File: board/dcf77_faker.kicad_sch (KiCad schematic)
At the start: 46 parts, among them J1 Barrel_Jack, J2 DBG, J3 ANT, J4 LCD_I2C, SW1 RST, SW2 H, SW3 MIN, SW4 S, U1 NCP1117ST33T3G, U2 ATSAML21G18B-AUT, X1 32.768kHz, X2 31MHz

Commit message: hand-solder X2, fix newly-detected DRC violations
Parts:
- X2: footprint Oscillator_Microchip:Oscillator_SMD_Microchip_DSC8001A-6Pin_7.0x5.0mm -> Oscillator_Microchip:Oscillator_SMD_Microchip_DSC8001A-6Pin_7.0x5.0mm_HandSolder
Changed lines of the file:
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@@
 (kicad_sch (version 20230121) (generator eeschema)
   (paper "A4")
+  (bus_alias "VIN" (members "VDDIN" "VSW" "VDDCORE" "VDDIO1" "VDDIO2" "VDDANA"))
+  (bus_alias "SWD" (members "SWDIO" "SWCLK" "~{RST}"))
   (bus_alias "BTN" (members "H" "MIN" "S"))
-  (bus_alias "VIN" (members "VDDIN" "VSW" "VDDCORE" "VDDIO1" "VDDIO2" "VDDANA"))
   (bus_alias "TWI0" (members "SDA0" "SCL0"))
-  (bus_alias "SWD" (members "SWDIO" "SWCLK" "~{RST}"))
   (junction (at 251.46 45.72) (diameter 0) (color 0 0 0 0)
   )
@@
       (effects (font (size 1.27 1.27)))
     )
-    (property "Footprint" "Oscillator_Microchip:Oscillator_SMD_Microchip_DSC8001A-6Pin_7.0x5.0mm" (at 243.84 130.81 0)
-      (effects (font (size 1.27 1.27)) hide)
-    )
+    (property "Footprint" "Oscillator_Microchip:Oscillator_SMD_Microchip_DSC8001A-6Pin_7.0x5.0mm_HandSolder" (at 243.84 130.81 0)
+      (effects (font (size 1.27 1.27)) hide)
+    )

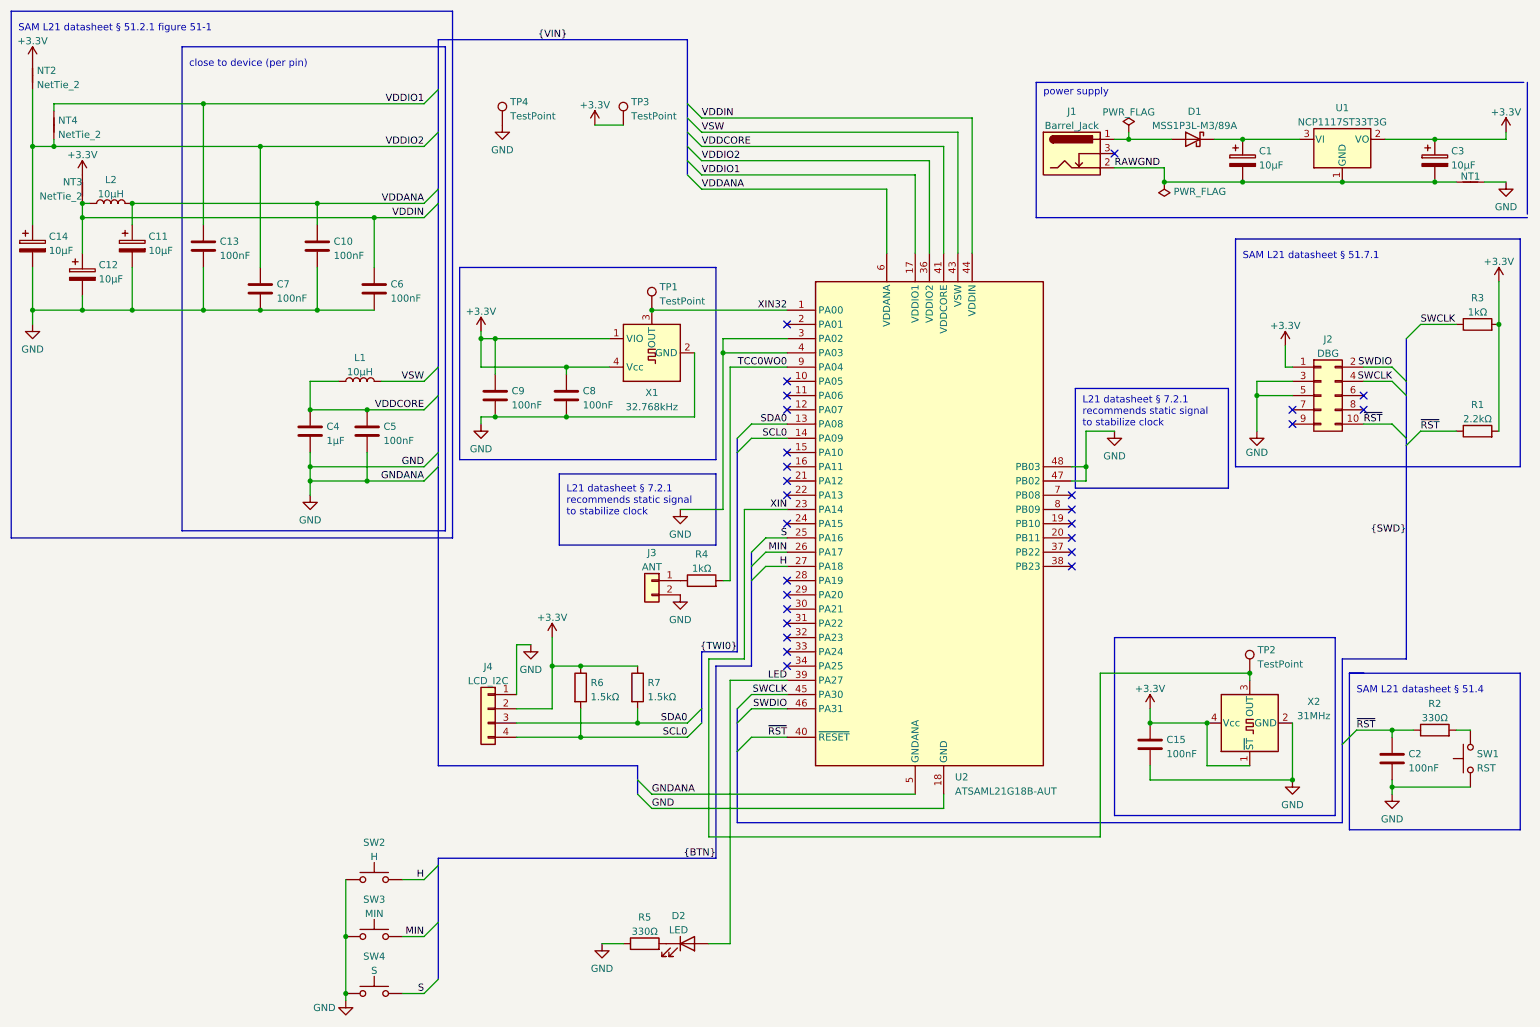
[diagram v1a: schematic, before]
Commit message: board: allow disabling X2
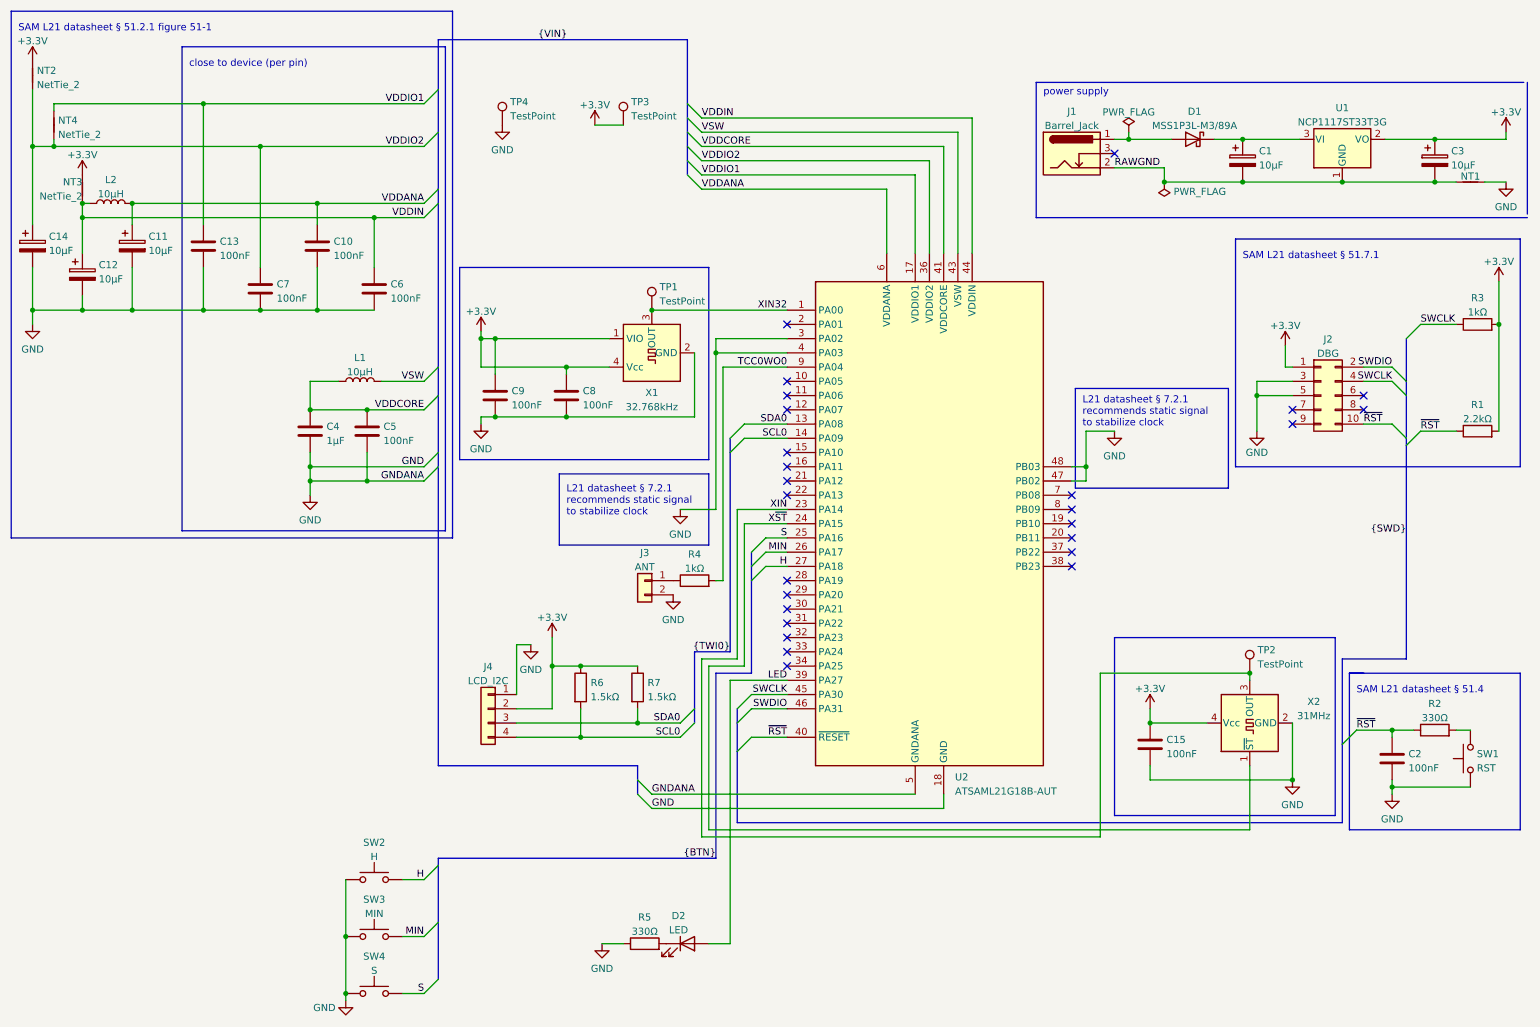
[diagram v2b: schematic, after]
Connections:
- net +3.3V: no longer X2.1 (~{ST})
- net X~{ST}: now reaches U2.24 (PA15)
- net X~{ST}: now also X2.1 (~{ST})
- no-connect marks 27 -> 26
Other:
- moved on the sheet: J3, R4

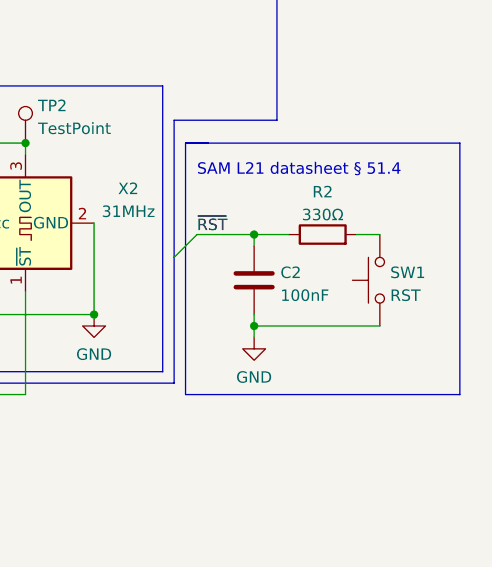
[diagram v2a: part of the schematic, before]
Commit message: board: move RST to make space for battery input
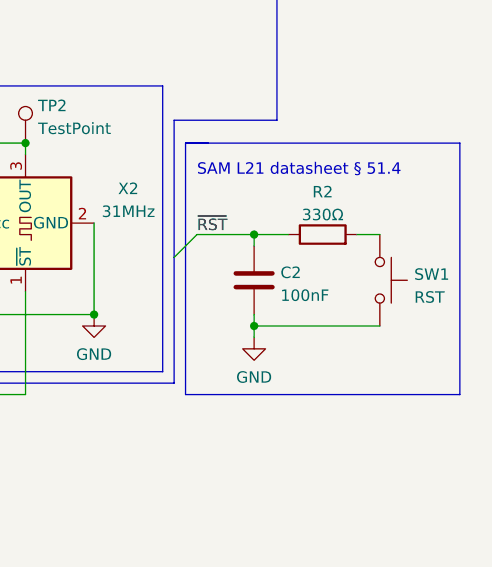
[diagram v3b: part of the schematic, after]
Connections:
- net GND: now also SW1.2; no longer SW1.1
- net at R2.2: now also SW1.1; no longer SW1.2
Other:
- moved on the sheet: SW1
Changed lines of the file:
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@@
     )
   )
-  (symbol (lib_id "Switch:SW_Push") (at 274.32 148.59 90) (unit 1)
+  (symbol (lib_id "Switch:SW_Push") (at 274.32 148.59 270) (unit 1)
     (in_bom yes) (on_board yes) (dnp no) (fields_autoplaced)
-    (property "Reference" "SW1" (at 275.463 147.7553 90)
-      (effects (font (size 1.27 1.27)) (justify right))
+    (property "Reference" "SW1" (at 278.13 147.955 90)
+      (effects (font (size 1.27 1.27)) (justify left))
     )
-    (property "Value" "RST" (at 275.463 150.2922 90)
-      (effects (font (size 1.27 1.27)) (justify right))
+    (property "Value" "RST" (at 278.13 150.495 90)
+      (effects (font (size 1.27 1.27)) (justify left))
     )
-    (property "Footprint" "Button_Switch_SMD_Side:Shou_Han_TS24CA" (at 269.24 148.59 0)
+    (property "Footprint" "Button_Switch_SMD_Side:Shou_Han_TS24CA" (at 279.4 148.59 0)
       (effects (font (size 1.27 1.27)) hide)
     )
-    (property "Datasheet" "~" (at 269.24 148.59 0)
+    (property "Datasheet" "~" (at 279.4 148.59 0)
       (effects (font (size 1.27 1.27)) hide)
     )
